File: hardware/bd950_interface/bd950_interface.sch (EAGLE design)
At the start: 34 parts, among them IC1 FT4232HL, IC2 MAX208ECWG, IC3 4050D, IC4 AT93C46A-10SQ-2.7, IC5 786TV, X1 ECG.0B.304.CLV

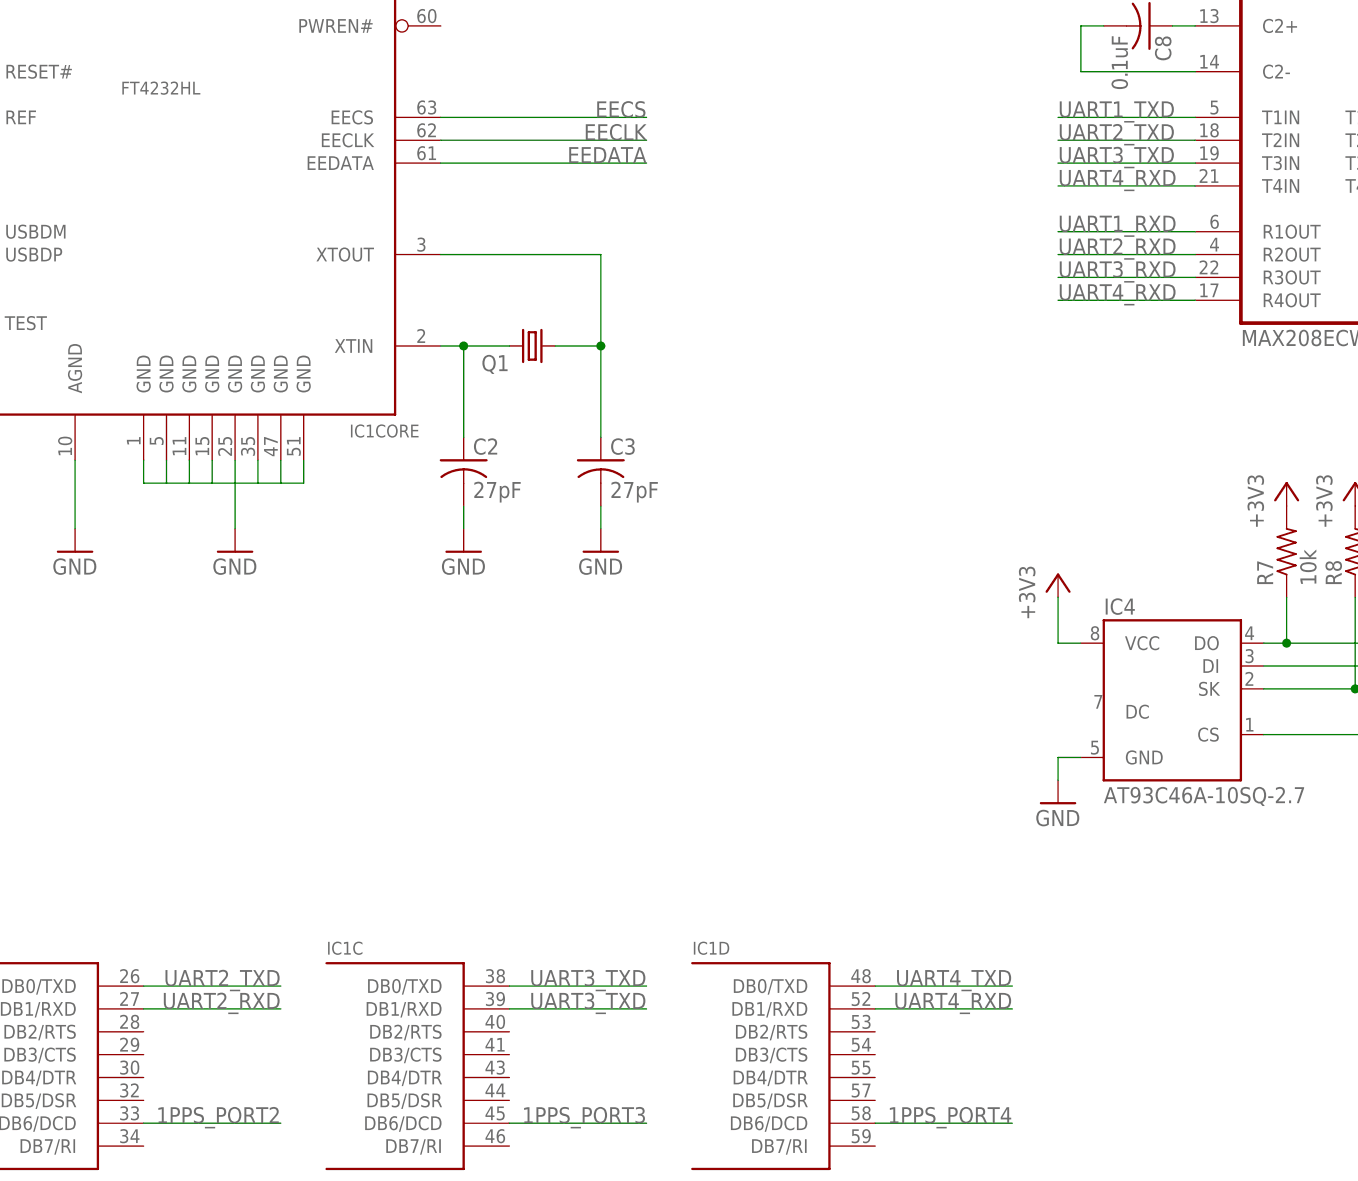
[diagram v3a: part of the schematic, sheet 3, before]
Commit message: Finish laying out BD950 interface board
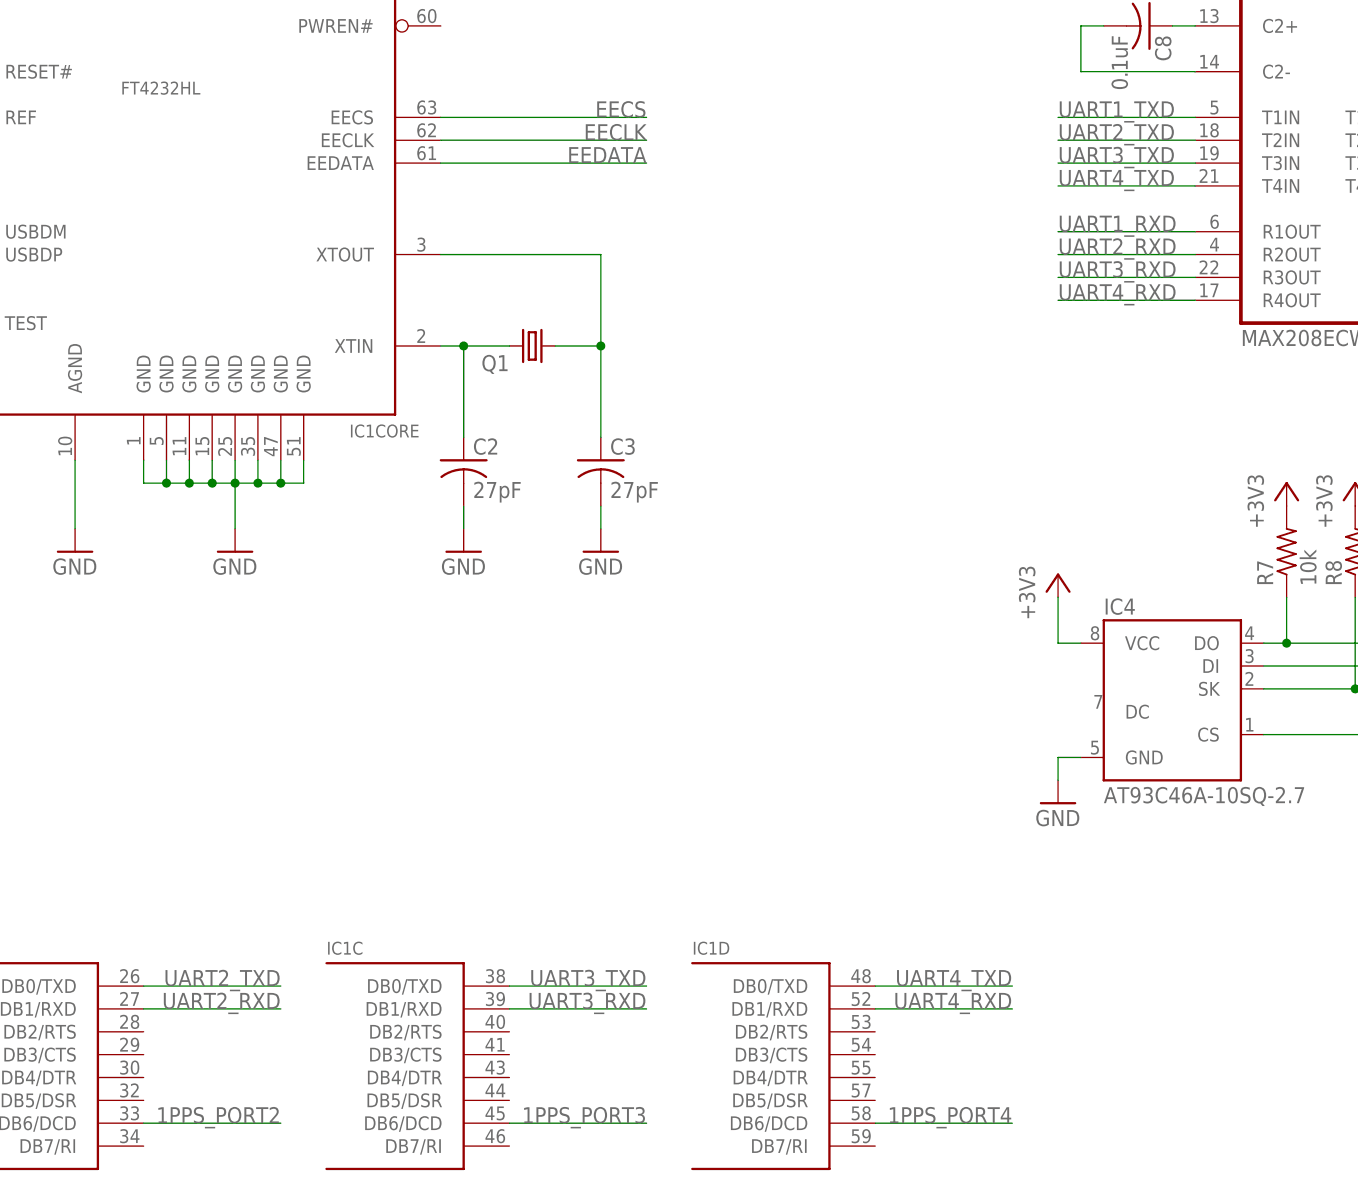
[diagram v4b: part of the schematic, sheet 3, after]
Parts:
- C4, C5: device resistor:C-USC0603 -> resistor:C-USC0805
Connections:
- removed net N$2: C5.1, IC5.VI
- net UART3_RXD: now also IC1C.DB1/RXD
- net UART3_TXD: no longer IC1C.DB1/RXD
- net UART4_RXD: no longer IC2G$1.T4IN
- net UART4_TXD: now also IC2G$1.T4IN
- net VDD: now also C5.1, IC5.VI
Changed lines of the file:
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@@
 <part name="IC5" library="linear" deviceset="78*" device="TV" technology="6"/>
 <part name="+3V9" library="supply1" deviceset="+3V3" device=""/>
-<part name="C4" library="resistor" deviceset="C-US" device="C0603" value="10uF"/>
+<part name="C4" library="resistor" deviceset="C-US" device="C0805" value="10uF"/>
 <part name="GND15" library="supply1" deviceset="GND" device=""/>
 <part name="GND16" library="supply1" deviceset="GND" device=""/>
-<part name="C5" library="resistor" deviceset="C-US" device="C0603" value="10uF"/>
+<part name="C5" library="resistor" deviceset="C-US" device="C0805" value="10uF"/>
 <part name="GND17" library="supply1" deviceset="GND" device=""/>
 <part name="R12" library="resistor" deviceset="R-US_" device="R0603" value="1k"/>
@@
 <pinref part="GND44" gate="1" pin="GND"/>
 <wire x1="83.82" y1="91.44" x2="83.82" y2="86.36" width="0.1524" layer="91"/>
+<junction x="76.2" y="91.44"/>
+<junction x="78.74" y="91.44"/>
+<junction x="81.28" y="91.44"/>
+<junction x="83.82" y="91.44"/>
+<junction x="86.36" y="91.44"/>
+<junction x="88.9" y="91.44"/>
 </segment>
 <segment>
@@
 <label x="170.18" y="35.56" size="1.778" layer="95" rot="MR0"/>
 </segment>
+<segment>
+<pinref part="IC2" gate="G$1" pin="T4IN"/>
+<wire x1="190.5" y1="124.46" x2="175.26" y2="124.46" width="0.1524" layer="91"/>
+<label x="175.26" y="124.46" size="1.778" layer="95"/>
+</segment>
 </net>
 <net name="UART4_RXD" class="0">
@@
 </segment>
 <segment>
-<pinref part="IC2" gate="G$1" pin="T4IN"/>
-<wire x1="190.5" y1="124.46" x2="175.26" y2="124.46" width="0.1524" layer="91"/>
-<label x="175.26" y="124.46" size="1.778" layer="95"/>
-</segment>
-<segment>
 <pinref part="IC2" gate="G$1" pin="R4OUT"/>
 <wire x1="190.5" y1="111.76" x2="175.26" y2="111.76" width="0.1524" layer="91"/>
@@
 </segment>
 <segment>
+<pinref part="IC2" gate="G$1" pin="T3IN"/>
+<wire x1="190.5" y1="127" x2="175.26" y2="127" width="0.1524" layer="91"/>
+<label x="175.26" y="127" size="1.778" layer="95"/>
+</segment>
+</net>
+<net name="UART3_RXD" class="0">
+<segment>
+<pinref part="IC2" gate="G$1" pin="R3OUT"/>
+<wire x1="190.5" y1="114.3" x2="175.26" y2="114.3" width="0.1524" layer="91"/>
+<label x="175.26" y="114.3" size="1.778" layer="95"/>
+</segment>
+<segment>
 <pinref part="IC1" gate="C" pin="DB1/RXD"/>
 <wire x1="114.3" y1="33.02" x2="129.54" y2="33.02" width="0.1524" layer="91"/>
 <label x="129.54" y="33.02" size="1.778" layer="95" rot="MR0"/>
-</segment>
-<segment>
-<pinref part="IC2" gate="G$1" pin="T3IN"/>
-<wire x1="190.5" y1="127" x2="175.26" y2="127" width="0.1524" layer="91"/>
-<label x="175.26" y="127" size="1.778" layer="95"/>
-</segment>
-</net>
-<net name="UART3_RXD" class="0">
-<segment>
-<pinref part="IC2" gate="G$1" pin="R3OUT"/>
-<wire x1="190.5" y1="114.3" x2="175.26" y2="114.3" width="0.1524" layer="91"/>
-<label x="175.26" y="114.3" size="1.778" layer="95"/>
 </segment>
 </net>
@@
 </segment>
 </net>
-<net name="N$2" class="0">
+<net name="USB_D-" class="0">
+<segment>
+<pinref part="IC1" gate="CORE" pin="USBDM"/>
+<wire x1="50.8" y1="119.38" x2="10.16" y2="119.38" width="0.1524" layer="91"/>
+<label x="10.16" y="119.38" size="1.778" layer="95"/>
+</segment>
+</net>
+<net name="USB_D+" class="0">
+<segment>
+<pinref part="IC1" gate="CORE" pin="USBDP"/>
+<wire x1="50.8" y1="116.84" x2="10.16" y2="116.84" width="0.1524" layer="91"/>
+<label x="10.16" y="116.84" size="1.778" layer="95"/>
+</segment>
+</net>
+<net name="N$16" class="0">
+<segment>
+<wire x1="177.8" y1="152.4" x2="177.8" y2="147.32" width="0.1524" layer="91"/>
+<pinref part="IC2" gate="G$1" pin="C1-"/>
+<wire x1="177.8" y1="147.32" x2="190.5" y2="147.32" width="0.1524" layer="91"/>
+<pinref part="C6" gate="G$1" pin="2"/>
+<wire x1="180.34" y1="152.4" x2="177.8" y2="152.4" width="0.1524" layer="91"/>
+</segment>
+</net>
+<net name="N$14" class="0">
+<segment>
+<pinref part="C6" gate="G$1" pin="1"/>
+<pinref part="IC2" gate="G$1" pin="C1+"/>
+<wire x1="187.96" y1="152.4" x2="190.5" y2="152.4" width="0.1524" layer="91"/>
+</segment>
+</net>
+<net name="N$17" class="0">
+<segment>
+<pinref part="C8" gate="G$1" pin="1"/>
+<pinref part="IC2" gate="G$1" pin="C2+"/>
+<wire x1="187.96" y1="142.24" x2="190.5" y2="142.24" width="0.1524" layer="91"/>
+</segment>
+</net>
+<net name="N$18" class="0">
+<segment>
+<pinref part="IC2" gate="G$1" pin="C2-"/>
+<wire x1="190.5" y1="137.16" x2="177.8" y2="137.16" width="0.1524" layer="91"/>
+<wire x1="177.8" y1="137.16" x2="177.8" y2="142.24" width="0.1524" layer="91"/>
+<pinref part="C8" gate="G$1" pin="2"/>
+<wire x1="177.8" y1="142.24" x2="180.34" y2="142.24" width="0.1524" layer="91"/>
+</segment>
+</net>
+<net name="N$19" class="0">
+<segment>
+<pinref part="IC2" gate="G$1" pin="V-"/>
+<wire x1="220.98" y1="144.78" x2="223.52" y2="144.78" width="0.1524" layer="91"/>
+<wire x1="223.52" y1="144.78" x2="223.52" y2="139.7" width="0.1524" layer="91"/>
+<pinref part="C9" gate="G$1" pin="1"/>
+<wire x1="223.52" y1="139.7" x2="231.14" y2="139.7" width="0.1524" layer="91"/>
+</segment>
+</net>
+<net name="N$20" class="0">
+<segment>
+<pinref part="IC2" gate="G$1" pin="V+"/>
+<wire x1="220.98" y1="149.86" x2="223.52" y2="149.86" width="0.1524" layer="91"/>
+<wire x1="223.52" y1="149.86" x2="223.52" y2="154.94" width="0.1524" layer="91"/>
+<pinref part="C10" gate="G$1" pin="1"/>
+<wire x1="223.52" y1="154.94" x2="231.14" y2="154.94" width="0.1524" layer="91"/>
+</segment>
+</net>
+<net name="PORT1_TXD" class="0">
+<segment>
+<pinref part="IC2" gate="G$1" pin="R1IN"/>
+<wire x1="220.98" y1="119.38" x2="238.76" y2="119.38" width="0.1524" layer="91"/>
+<label x="238.76" y="119.38" size="1.778" layer="95" rot="MR0"/>
+</segment>
+</net>
+<net name="PORT2_TXD" class="0">
+<segment>
+<pinref part="IC2" gate="G$1" pin="R2IN"/>
+<wire x1="220.98" y1="116.84" x2="238.76" y2="116.84" width="0.1524" layer="91"/>
+<label x="238.76" y="116.84" size="1.778" layer="95" rot="MR0"/>
+</segment>
+</net>
+<net name="PORT3_TXD" class="0">
+<segment>
+<pinref part="IC2" gate="G$1" pin="R3IN"/>
+<wire x1="220.98" y1="114.3" x2="238.76" y2="114.3" width="0.1524" layer="91"/>
+<label x="238.76" y="114.3" size="1.778" layer="95" rot="MR0"/>
+</segment>
+</net>
+<net name="VDD" class="0">
 <segment>
 <pinref part="C5" gate="G$1" pin="1"/>
@@
 <wire x1="200.66" y1="193.04" x2="193.04" y2="193.04" width="0.1524" layer="91"/>
 <junction x="193.04" y="193.04"/>
-</segment>
-</net>
-<net name="USB_D-" class="0">
-<segment>
-<pinref part="IC1" gate="CORE" pin="USBDM"/>
-<wire x1="50.8" y1="119.38" x2="10.16" y2="119.38" width="0.1524" layer="91"/>
-<label x="10.16" y="119.38" size="1.778" layer="95"/>
-</segment>
-</net>
-<net name="USB_D+" class="0">
-<segment>
-<pinref part="IC1" gate="CORE" pin="USBDP"/>
-<wire x1="50.8" y1="116.84" x2="10.16" y2="116.84" width="0.1524" layer="91"/>
-<label x="10.16" y="116.84" size="1.778" layer="95"/>
-</segment>
-</net>
-<net name="N$16" class="0">
-<segment>
-<wire x1="177.8" y1="152.4" x2="177.8" y2="147.32" width="0.1524" layer="91"/>
-<pinref part="IC2" gate="G$1" pin="C1-"/>
-<wire x1="177.8" y1="147.32" x2="190.5" y2="147.32" width="0.1524" layer="91"/>
-<pinref part="C6" gate="G$1" pin="2"/>
-<wire x1="180.34" y1="152.4" x2="177.8" y2="152.4" width="0.1524" layer="91"/>
-</segment>
-</net>
-<net name="N$14" class="0">
-<segment>
-<pinref part="C6" gate="G$1" pin="1"/>
-<pinref part="IC2" gate="G$1" pin="C1+"/>
-<wire x1="187.96" y1="152.4" x2="190.5" y2="152.4" width="0.1524" layer="91"/>
-</segment>
-</net>
-<net name="N$17" class="0">
-<segment>
-<pinref part="C8" gate="G$1" pin="1"/>
-<pinref part="IC2" gate="G$1" pin="C2+"/>
-<wire x1="187.96" y1="142.24" x2="190.5" y2="142.24" width="0.1524" layer="91"/>
-</segment>
-</net>
-<net name="N$18" class="0">
-<segment>
-<pinref part="IC2" gate="G$1" pin="C2-"/>
-<wire x1="190.5" y1="137.16" x2="177.8" y2="137.16" width="0.1524" layer="91"/>
-<wire x1="177.8" y1="137.16" x2="177.8" y2="142.24" width="0.1524" layer="91"/>
-<pinref part="C8" gate="G$1" pin="2"/>
-<wire x1="177.8" y1="142.24" x2="180.34" y2="142.24" width="0.1524" layer="91"/>
-</segment>
-</net>
-<net name="N$19" class="0">
-<segment>
-<pinref part="IC2" gate="G$1" pin="V-"/>
-<wire x1="220.98" y1="144.78" x2="223.52" y2="144.78" width="0.1524" layer="91"/>
-<wire x1="223.52" y1="144.78" x2="223.52" y2="139.7" width="0.1524" layer="91"/>
-<pinref part="C9" gate="G$1" pin="1"/>
-<wire x1="223.52" y1="139.7" x2="231.14" y2="139.7" width="0.1524" layer="91"/>
-</segment>
-</net>
-<net name="N$20" class="0">
-<segment>
-<pinref part="IC2" gate="G$1" pin="V+"/>
-<wire x1="220.98" y1="149.86" x2="223.52" y2="149.86" width="0.1524" layer="91"/>
-<wire x1="223.52" y1="149.86" x2="223.52" y2="154.94" width="0.1524" layer="91"/>
-<pinref part="C10" gate="G$1" pin="1"/>
-<wire x1="223.52" y1="154.94" x2="231.14" y2="154.94" width="0.1524" layer="91"/>
-</segment>
-</net>
-<net name="PORT1_TXD" class="0">
-<segment>
-<pinref part="IC2" gate="G$1" pin="R1IN"/>
-<wire x1="220.98" y1="119.38" x2="238.76" y2="119.38" width="0.1524" layer="91"/>
-<label x="238.76" y="119.38" size="1.778" layer="95" rot="MR0"/>
-</segment>
-</net>
-<net name="PORT2_TXD" class="0">
-<segment>
-<pinref part="IC2" gate="G$1" pin="R2IN"/>
-<wire x1="220.98" y1="116.84" x2="238.76" y2="116.84" width="0.1524" layer="91"/>
-<label x="238.76" y="116.84" size="1.778" layer="95" rot="MR0"/>
-</segment>
-</net>
-<net name="PORT3_TXD" class="0">
-<segment>
-<pinref part="IC2" gate="G$1" pin="R3IN"/>
-<wire x1="220.98" y1="114.3" x2="238.76" y2="114.3" width="0.1524" layer="91"/>
-<label x="238.76" y="114.3" size="1.778" layer="95" rot="MR0"/>
-</segment>
-</net>
+<pinref part="VDD4" gate="G$1" pin="VDD"/>
+</segment>
+</net>
